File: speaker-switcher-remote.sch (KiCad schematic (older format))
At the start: 26 parts, among them M1 arduino-nano, Q1 2N2222, Q2 TIP31C, U1 LM7805_TO220

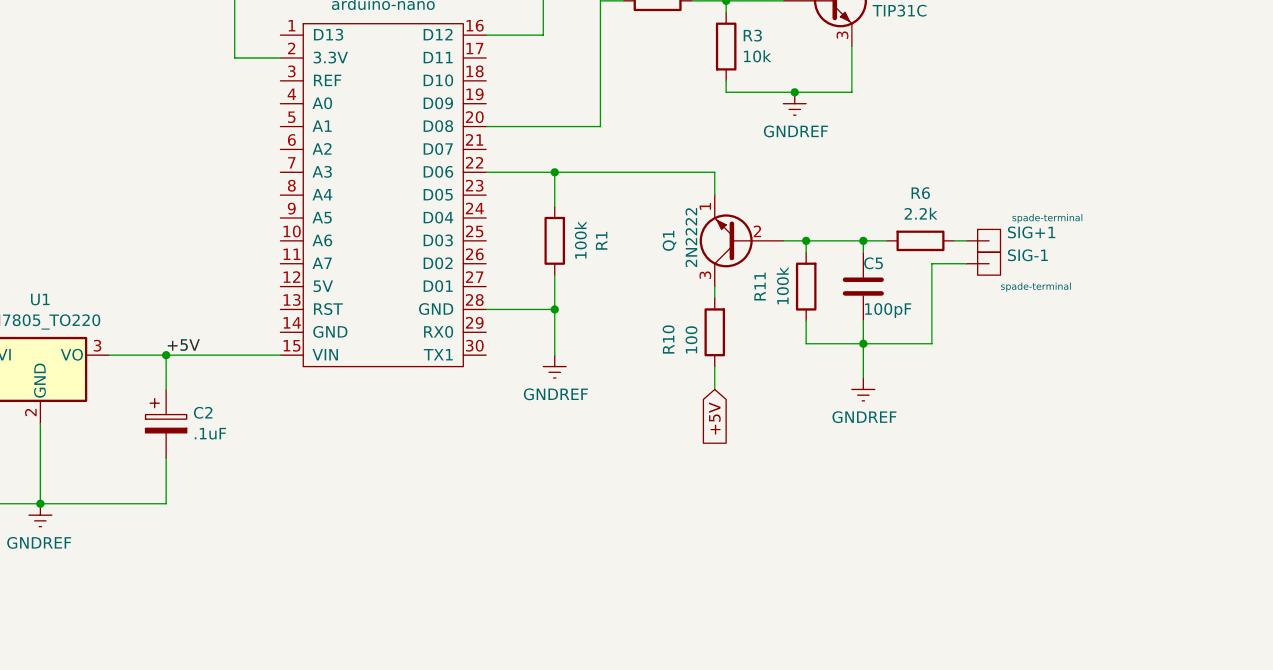
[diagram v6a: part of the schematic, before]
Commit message: Updated board as per Dan's remarks
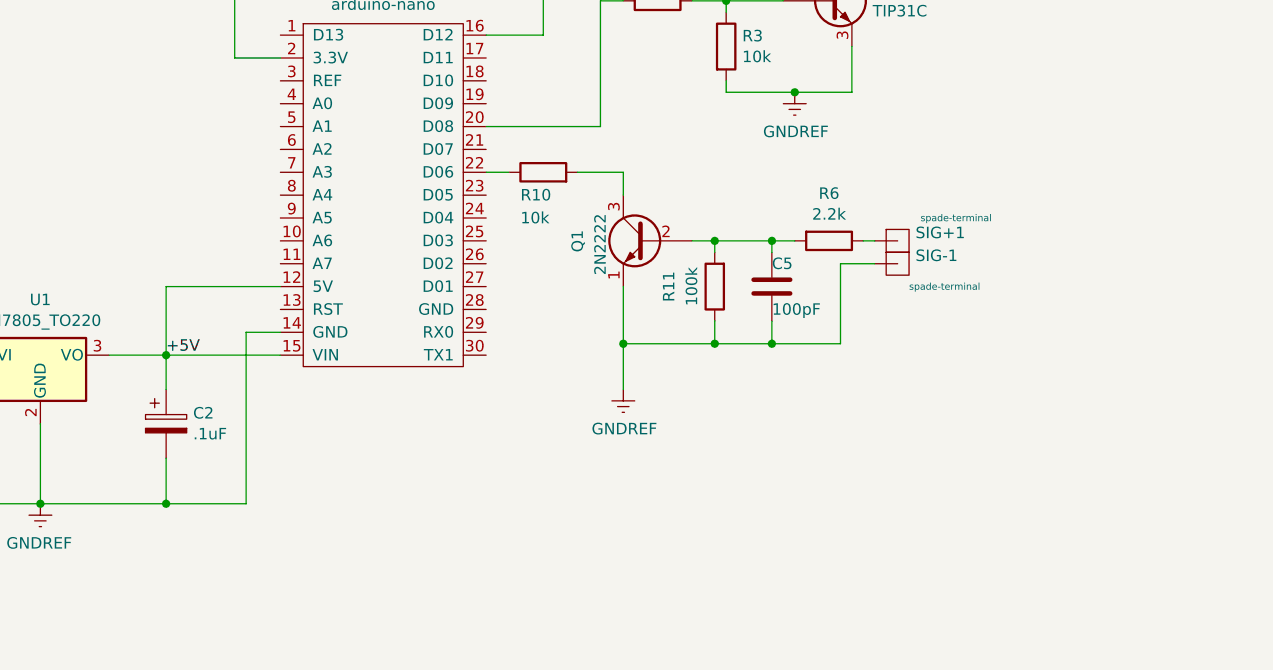
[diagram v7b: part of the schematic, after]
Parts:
- removed R1: 100k, Resistor_THT:R_Axial_DIN0207_L6.3mm_D2.5mm_P7.62mm_Horizontal, symbol Device:R
- R10: value 100 -> 10k
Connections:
- net +5V: now also M1.12 (5V); no longer R10.1
- net GNDREF: now also M1.14 (GND), Q1.1 (E); no longer M1.28 (GND)
- net at M1.22 (D06): now also R10.1; no longer Q1.1 (E)
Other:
- moved on the sheet: C5, Q1, R10, R11, R6, SIG+1, SIG-1
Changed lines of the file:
@@
 	0    1    1    0
 $EndComp
-Wire Wire Line
-	6350 4750 6050 4750
 $Comp
 L Device:Q_NPN_BCE Q2
@@
 $EndComp
 $Comp
-L power:GNDREF #PWR0102
-U 1 1 60071496
-P 6350 4950
-F 0 "#PWR0102" H 6350 4700 50  0001 C CNN
-F 1 "GNDREF" H 6355 4777 50  0000 C CNN
-F 2 "" H 6350 4950 50  0001 C CNN
-F 3 "" H 6350 4950 50  0001 C CNN
-	1    6350 4950
-	1    0    0    -1
-$EndComp
-$Comp
 L power:GNDREF #PWR0105
 U 1 1 60085B7D
@@
 $EndComp
 $Comp
-L Device:R R1
-U 1 1 60064471
-P 6350 4450
-F 0 "R1" V 6143 4450 50  0000 C CNN
-F 1 "100k" V 6234 4450 50  0000 C CNN
-F 2 "Resistor_THT:R_Axial_DIN0207_L6.3mm_D2.5mm_P7.62mm_Horizontal" V 6280 4450 50  0001 C CNN
-F 3 "~" H 6350 4450 50  0001 C CNN
-	1    6350 4450
-	-1   0    0    1
-$EndComp
-$Comp
 L power:GNDREF #PWR0106
 U 1 1 600E3B6B
-P 7700 5050
-F 0 "#PWR0106" H 7700 4800 50  0001 C CNN
-F 1 "GNDREF" H 7705 4877 50  0000 C CNN
-F 2 "" H 7700 5050 50  0001 C CNN
-F 3 "" H 7700 5050 50  0001 C CNN
-	1    7700 5050
+P 6650 5100
+F 0 "#PWR0106" H 6650 4850 50  0001 C CNN
+F 1 "GNDREF" H 6655 4927 50  0000 C CNN
+F 2 "" H 6650 5100 50  0001 C CNN
+F 3 "" H 6650 5100 50  0001 C CNN
+	1    6650 5100
 	1    0    0    -1
 $EndComp
@@
 L speaker-switcher-remote-rescue:spade-terminal-arduino SIG-1
 U 1 1 600B1A54
-P 8250 4550
-F 0 "SIG-1" H 8328 4585 50  0000 L CNN
-F 1 "spade-terminal" H 8300 4450 30  0000 L CNN
-F 2 "arduino-nano:SpadeTerminal635" H 8100 4700 50  0001 C CNN
-F 3 "" H 8100 4700 50  0001 C CNN
-	1    8250 4550
+P 7850 4550
+F 0 "SIG-1" H 7928 4585 50  0000 L CNN
+F 1 "spade-terminal" H 7900 4450 30  0000 L CNN
+F 2 "arduino-nano:SpadeTerminal635" H 7700 4700 50  0001 C CNN
+F 3 "" H 7700 4700 50  0001 C CNN
+	1    7850 4550
 	1    0    0    -1
 $EndComp
@@
 L speaker-switcher-remote-rescue:spade-terminal-arduino SIG+1
 U 1 1 600B3081
-P 8250 4450
-F 0 "SIG+1" H 8328 4485 50  0000 L CNN
-F 1 "spade-terminal" H 8350 4550 30  0000 L CNN
-F 2 "arduino-nano:SpadeTerminal635" H 8100 4600 50  0001 C CNN
-F 3 "" H 8100 4600 50  0001 C CNN
-	1    8250 4450
+P 7850 4450
+F 0 "SIG+1" H 7928 4485 50  0000 L CNN
+F 1 "spade-terminal" H 7950 4550 30  0000 L CNN
+F 2 "arduino-nano:SpadeTerminal635" H 7700 4600 50  0001 C CNN
+F 3 "" H 7700 4600 50  0001 C CNN
+	1    7850 4450
 	1    0    0    -1
 $EndComp
@@
 	4650 5600 4650 5400
 Connection ~ 4100 5600
-Wire Wire Line
-	4100 5600 4650 5600
 Connection ~ 4650 4950
 Wire Wire Line
@@
 	7650 3800 7400 3800
 Wire Wire Line
-	6050 4150 6350 4150
-Wire Wire Line
-	6350 4150 6350 4300
-Connection ~ 6350 4150
-Wire Wire Line
-	6350 4600 6350 4750
-Connection ~ 6350 4750
-Wire Wire Line
 	6550 3400 6550 3950
-Wire Wire Line
-	6350 4150 7050 4150
-Text GLabel 7050 5100 3    50   Input ~ 0
-+5V
 Wire Wire Line
 	6300 2150 6250 2150
@@
 L Device:R R6
 U 1 1 600BEA2A
-P 7950 4450
-F 0 "R6" V 7743 4450 50  0000 C CNN
-F 1 "2.2k" V 7834 4450 50  0000 C CNN
-F 2 "Resistor_THT:R_Axial_DIN0207_L6.3mm_D2.5mm_P7.62mm_Horizontal" V 7880 4450 50  0001 C CNN
-F 3 "~" H 7950 4450 50  0001 C CNN
-	1    7950 4450
+P 7550 4450
+F 0 "R6" V 7343 4450 50  0000 C CNN
+F 1 "2.2k" V 7434 4450 50  0000 C CNN
+F 2 "Resistor_THT:R_Axial_DIN0207_L6.3mm_D2.5mm_P7.62mm_Horizontal" V 7480 4450 50  0001 C CNN
+F 3 "~" H 7550 4450 50  0001 C CNN
+	1    7550 4450
 	0    1    1    0
 $EndComp
@@
 L Device:R R10
 U 1 1 603B8358
-P 7050 4850
-F 0 "R10" V 7250 4950 50  0000 R CNN
-F 1 "100" V 7150 4950 50  0000 R CNN
-F 2 "Resistor_THT:R_Axial_DIN0207_L6.3mm_D2.5mm_P7.62mm_Horizontal" V 6980 4850 50  0001 C CNN
-F 3 "~" H 7050 4850 50  0001 C CNN
-	1    7050 4850
-	-1   0    0    1
-$EndComp
-Wire Wire Line
-	7050 5000 7050 5100
+P 6300 4150
+F 0 "R10" V 6200 4250 50  0000 R CNN
+F 1 "10k" V 6100 4250 50  0000 R CNN
+F 2 "Resistor_THT:R_Axial_DIN0207_L6.3mm_D2.5mm_P7.62mm_Horizontal" V 6230 4150 50  0001 C CNN
+F 3 "~" H 6300 4150 50  0001 C CNN
+	1    6300 4150
+	0    -1   -1   0
+$EndComp
 Text Notes 7400 7500 0    63   ~ 0
 Speaker Swither Remote
@@
 0.1.0
 Wire Wire Line
-	7700 5050 7700 4900
-Connection ~ 7700 4900
-Wire Wire Line
-	8150 4550 8000 4550
-Wire Wire Line
-	8000 4550 8000 4900
-Wire Wire Line
-	8150 4450 8100 4450
-Wire Wire Line
-	7800 4450 7700 4450
+	6650 4900 7050 4900
+Connection ~ 7300 4900
+Wire Wire Line
+	7750 4550 7600 4550
+Wire Wire Line
+	7600 4550 7600 4900
+Wire Wire Line
+	7750 4450 7700 4450
+Wire Wire Line
+	7400 4450 7300 4450
 $Comp
 L Device:C C5
 U 1 1 60194B26
-P 7700 4650
-F 0 "C5" H 7700 4750 50  0000 L CNN
-F 1 "100pF" H 7700 4550 50  0000 L CNN
-F 2 "Capacitor_THT:C_Disc_D6.0mm_W2.5mm_P5.00mm" H 7738 4500 50  0001 C CNN
-F 3 "~" H 7700 4650 50  0001 C CNN
-	1    7700 4650
-	1    0    0    -1
-$EndComp
-Wire Wire Line
-	7700 4450 7700 4500
-Wire Wire Line
-	7700 4800 7700 4900
-Wire Wire Line
-	7700 4900 8000 4900
-Wire Wire Line
-	7050 4650 7050 4700
-Wire Wire Line
-	7050 4150 7050 4250
+P 7300 4650
+F 0 "C5" H 7300 4750 50  0000 L CNN
+F 1 "100pF" H 7300 4550 50  0000 L CNN
+F 2 "Capacitor_THT:C_Disc_D6.0mm_W2.5mm_P5.00mm" H 7338 4500 50  0001 C CNN
+F 3 "~" H 7300 4650 50  0001 C CNN
+	1    7300 4650
+	1    0    0    -1
+$EndComp
+Wire Wire Line
+	7300 4450 7300 4500
+Wire Wire Line
+	7300 4800 7300 4900
+Wire Wire Line
+	7300 4900 7600 4900
+Wire Wire Line
+	6650 4150 6650 4250
 $Comp
 L Device:R R11
 U 1 1 601695ED
-P 7450 4650
-F 0 "R11" V 7650 4650 50  0000 C CNN
-F 1 "100k" V 7550 4650 50  0000 C CNN
-F 2 "Resistor_THT:R_Axial_DIN0207_L6.3mm_D2.5mm_P7.62mm_Horizontal" V 7380 4650 50  0001 C CNN
-F 3 "~" H 7450 4650 50  0001 C CNN
-	1    7450 4650
+P 7050 4650
+F 0 "R11" V 7250 4650 50  0000 C CNN
+F 1 "100k" V 7150 4650 50  0000 C CNN
+F 2 "Resistor_THT:R_Axial_DIN0207_L6.3mm_D2.5mm_P7.62mm_Horizontal" V 6980 4650 50  0001 C CNN
+F 3 "~" H 7050 4650 50  0001 C CNN
+	1    7050 4650
 	-1   0    0    1
 $EndComp
@@
 L Device:Q_NPN_EBC Q1
 U 1 1 602A1BF3
-P 7150 4450
-F 0 "Q1" V 7450 4400 50  0000 L CNN
-F 1 "2N2222" V 7350 4300 50  0000 L CNN
-F 2 "Package_TO_SOT_THT:TO-92" H 7350 4550 50  0001 C CNN
-F 3 "~" H 7150 4450 50  0001 C CNN
-	1    7150 4450
-	-1   0    0    1
-$EndComp
-Wire Wire Line
-	7350 4450 7450 4450
-Connection ~ 7700 4450
-Wire Wire Line
-	7450 4500 7450 4450
-Connection ~ 7450 4450
-Wire Wire Line
-	7450 4450 7700 4450
-Wire Wire Line
-	7450 4800 7450 4900
-Wire Wire Line
-	7450 4900 7700 4900
+P 6750 4450
+F 0 "Q1" V 7050 4400 50  0000 L CNN
+F 1 "2N2222" V 6950 4300 50  0000 L CNN
+F 2 "Package_TO_SOT_THT:TO-92" H 6950 4550 50  0001 C CNN
+F 3 "~" H 6750 4450 50  0001 C CNN
+	1    6750 4450
+	-1   0    0    -1
+$EndComp
+Wire Wire Line
+	6950 4450 7050 4450
+Connection ~ 7300 4450
+Wire Wire Line
+	7050 4500 7050 4450
+Connection ~ 7050 4450
+Wire Wire Line
+	7050 4450 7300 4450
+Wire Wire Line
+	7050 4800 7050 4900
+Wire Wire Line
+	7050 4900 7300 4900
 Connection ~ 7400 3800
 Wire Wire Line
@@
 Wire Wire Line
 	6650 3400 6550 3400
-Wire Wire Line
-	6350 4750 6350 4950
 $Comp
 L Device:R R9
@@
 	0    -1   -1   0
 $EndComp
+Wire Wire Line
+	4650 4950 4650 4650
+Wire Wire Line
+	4650 4650 5150 4650
+Wire Wire Line
+	6050 4150 6150 4150
+Wire Wire Line
+	5150 4850 5000 4850
+Wire Wire Line
+	5000 4850 5000 5600
+Wire Wire Line
+	4100 5600 4650 5600
+Connection ~ 4650 5600
+Wire Wire Line
+	4650 5600 5000 5600
+Wire Wire Line
+	6450 4150 6650 4150
+Wire Wire Line
+	6650 4650 6650 4900
+Connection ~ 7050 4900
+Connection ~ 6650 4900
+Wire Wire Line
+	6650 4900 6650 5100
 $EndSCHEMATC

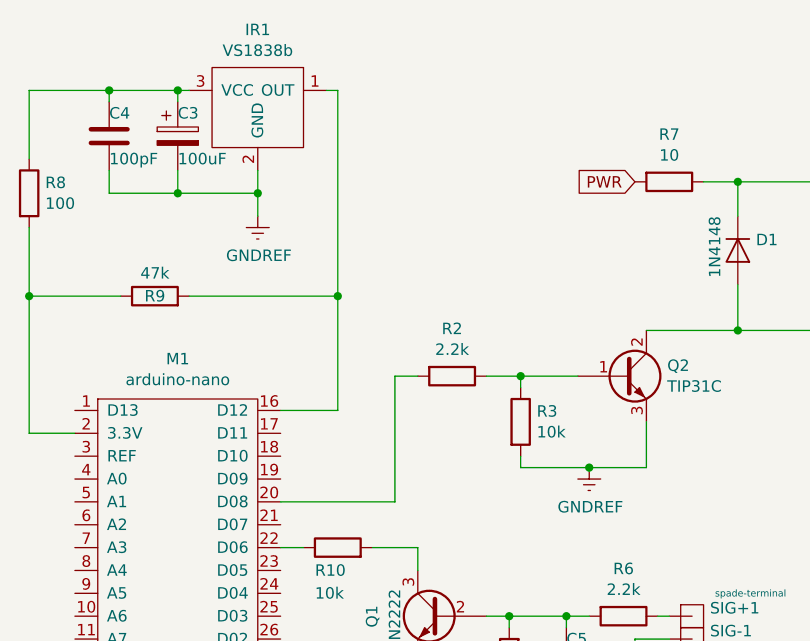
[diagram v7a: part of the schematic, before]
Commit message: Added indicator LED to d09
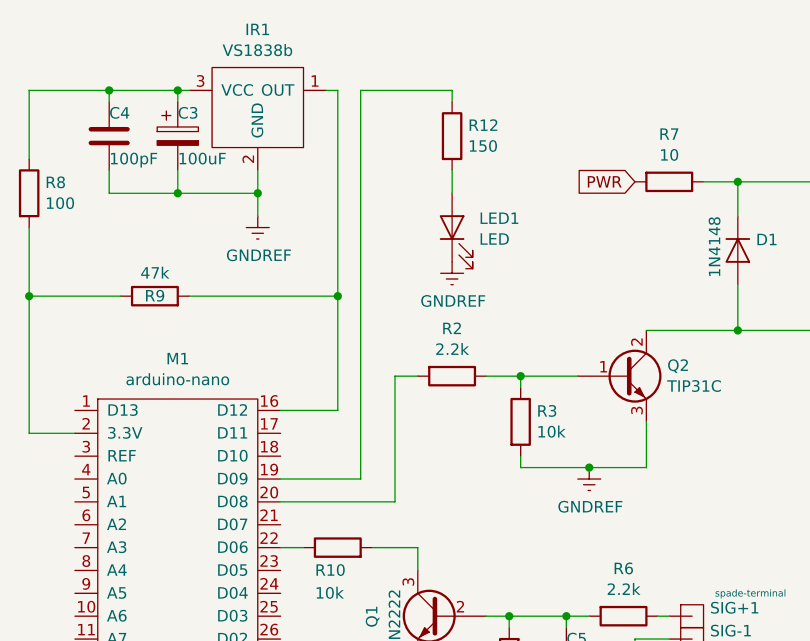
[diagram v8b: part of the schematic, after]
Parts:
- added LED1: LED, Connector_JST:JST_XH_B2B-XH-A_1x02_P2.50mm_Vertical, symbol Device:LED
- added R12: 150, Resistor_THT:R_Axial_DIN0207_L6.3mm_D2.5mm_P7.62mm_Horizontal, symbol Device:R
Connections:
- net GNDREF: now also LED1.1 (K)
- net at M1.19 (D09): now also R12.1
- new net: LED1.2 (A), R12.2
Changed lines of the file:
@@
 Wire Wire Line
 	6650 4900 6650 5100
+$Comp
+L Device:LED LED1
+U 1 1 6028FD00
+P 6800 2750
+F 0 "LED1" V 6839 2632 50  0000 R CNN
+F 1 "LED" V 6748 2632 50  0000 R CNN
+F 2 "Connector_JST:JST_XH_B2B-XH-A_1x02_P2.50mm_Vertical" H 6800 2750 50  0001 C CNN
+F 3 "~" H 6800 2750 50  0001 C CNN
+	1    6800 2750
+	0    -1   -1   0
+$EndComp
+$Comp
+L Device:R R12
+U 1 1 6029689B
+P 6800 2350
+F 0 "R12" H 6870 2396 50  0000 L CNN
+F 1 "150" H 6870 2305 50  0000 L CNN
+F 2 "Resistor_THT:R_Axial_DIN0207_L6.3mm_D2.5mm_P7.62mm_Horizontal" V 6730 2350 50  0001 C CNN
+F 3 "~" H 6800 2350 50  0001 C CNN
+	1    6800 2350
+	1    0    0    -1
+$EndComp
+Wire Wire Line
+	6800 2200 6800 2150
+Wire Wire Line
+	6800 2150 6400 2150
+Wire Wire Line
+	6400 2150 6400 3850
+Wire Wire Line
+	6400 3850 6050 3850
+Wire Wire Line
+	6800 2500 6800 2600
+$Comp
+L power:GNDREF #PWR0102
+U 1 1 6029E392
+P 6800 2900
+F 0 "#PWR0102" H 6800 2650 50  0001 C CNN
+F 1 "GNDREF" H 6805 2727 50  0000 C CNN
+F 2 "" H 6800 2900 50  0001 C CNN
+F 3 "" H 6800 2900 50  0001 C CNN
+	1    6800 2900
+	1    0    0    -1
+$EndComp
 $EndSCHEMATC
